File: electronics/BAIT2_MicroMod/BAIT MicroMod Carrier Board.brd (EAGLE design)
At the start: 92.7 x 80 mm, 156 parts, among them J1 SJ-43516-SMT, J10 QWIIC_RIGHT_ANGLE, J11 QWIIC_RIGHT_ANGLE, J15 BM05B-SRSS-TB(LF)(SN), J2 ST-TF-003A, J4 BM05B-SRSS-TB(LF)(SN), J5 QWIIC_RIGHT_ANGLE, J6 JST 2PH, J7 MICROMOD-2222-C, SW1 SKQGADE010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

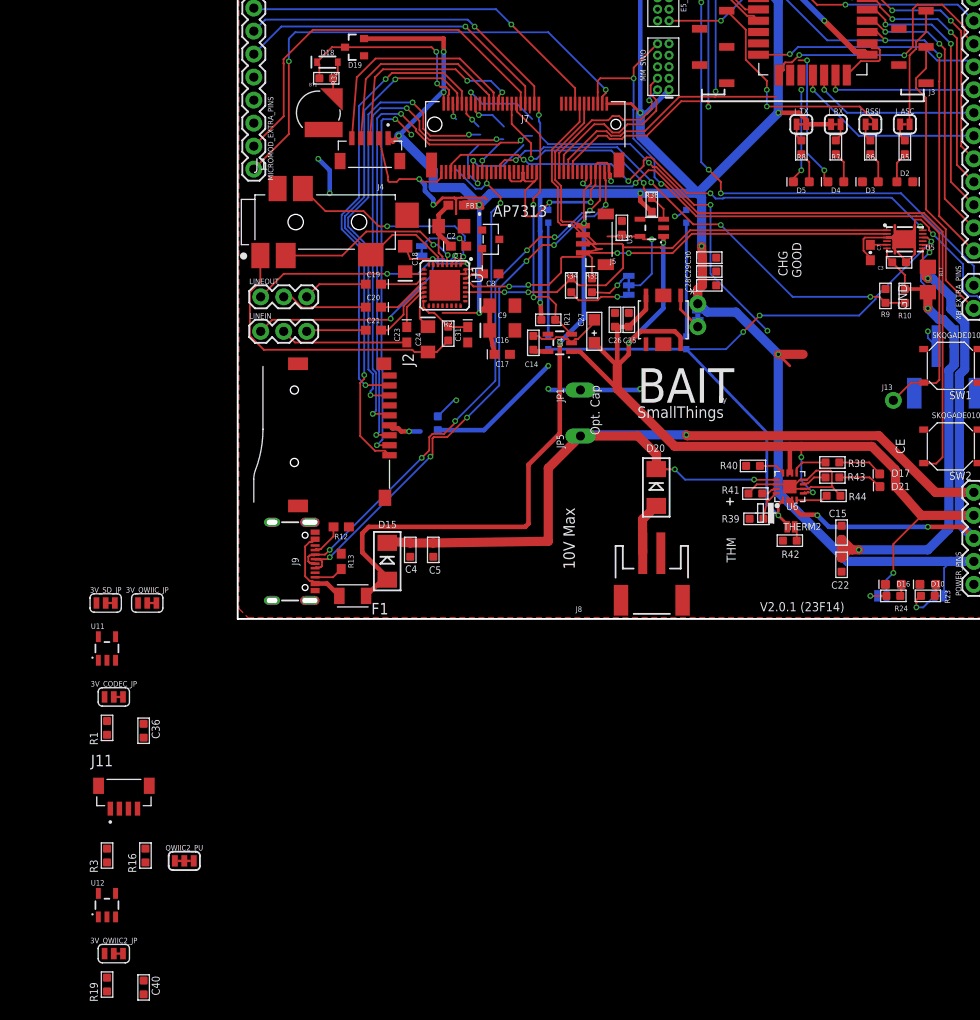
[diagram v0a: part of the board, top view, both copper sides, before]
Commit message: Connected SD card detect pin to micromod
Resolves #25
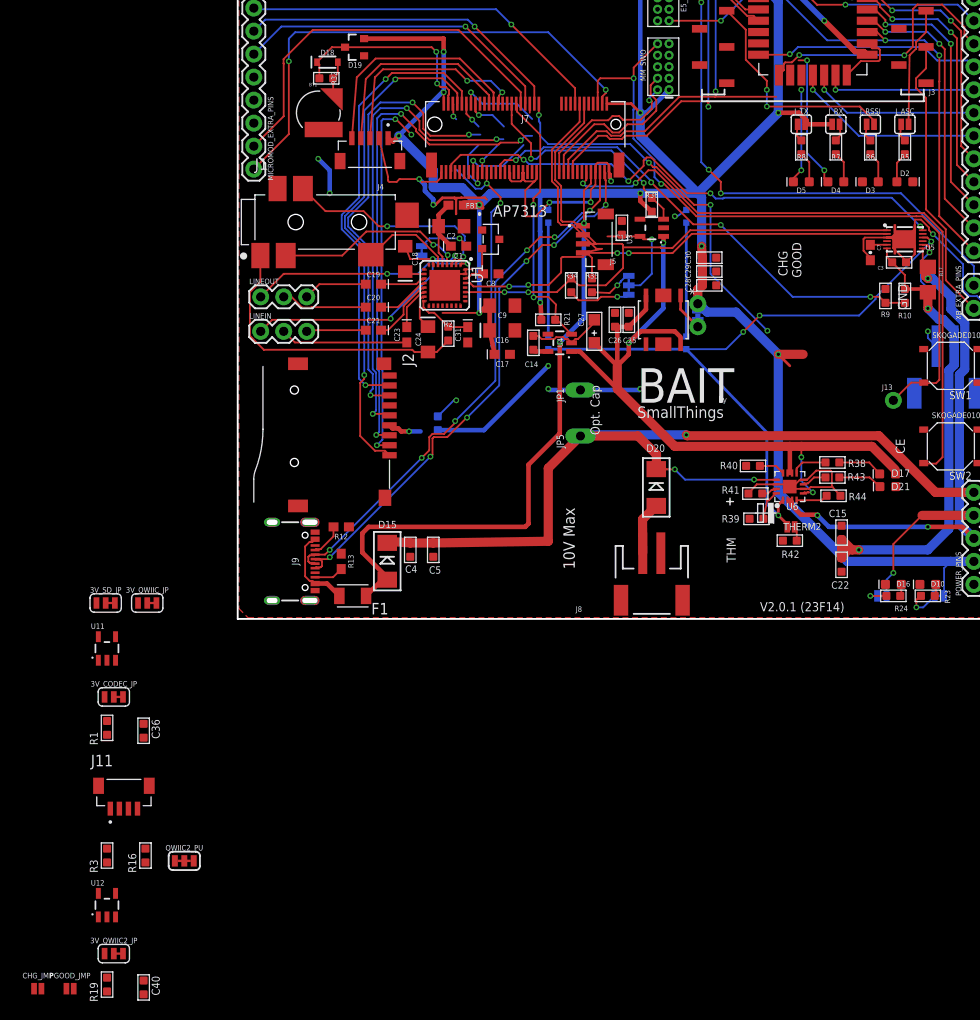
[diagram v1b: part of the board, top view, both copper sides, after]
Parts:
- added CHG_JMP, PGOOD_JMP: (no value), SparkFun-Jumpers:SMT-JUMPER_2_NO_NO-SILK
- J_ASC, J_RSSI, J_RX, J_TX: value (none) -> JUMPER-SMT_2_NO_SILK; device SparkFun-Jumpers:SMT-JUMPER_2_NC_TRACE_SILK -> SparkFun-Jumpers:SMT-JUMPER_2_NO_SILK
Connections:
- new net N$75: D21.A, PGOOD_JMP.1
- new net N$76: CHG_JMP.1, D17.A
- new net SD_DETECT: J2.9, J7.73
- net V+: now also CHG_JMP.2, PGOOD_JMP.2; no longer D17.A, D21.A
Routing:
- net V+: track 113.7 -> 107.5 mm
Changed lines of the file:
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@@
 <attribute name="NAME" x="19.251" y="75.865" size="0.889" layer="25" ratio="11" rot="R90"/>
 </element>
-<element name="J_ASC" library="SparkFun-Jumpers" package="SMT-JUMPER_2_NC_TRACE_SILK" package3d_urn="urn:adsk.eagle:package:39281/1" value="" x="73.66" y="54.61" smashed="yes" grouprefs="WIRELESS">
+<element name="J_ASC" library="SparkFun-Jumpers" library_urn="urn:adsk.eagle:library:528" package="SMT-JUMPER_2_NO_SILK" package3d_urn="urn:adsk.eagle:package:39279/1" value="JUMPER-SMT_2_NO_SILK" x="73.66" y="54.61" smashed="yes" grouprefs="WIRELESS">
 <attribute name="NAME" x="73.66" y="55.753" size="0.6096" layer="25" font="vector" ratio="20" align="bottom-center"/>
 <attribute name="VALUE" x="73.66" y="53.467" size="0.6096" layer="27" font="vector" ratio="20" align="top-center"/>
@@
 <attribute name="PROD_ID" value="HW-14899" x="137.414" y="-20.574" size="1.778" layer="27" display="off"/>
 </element>
-<element name="J_RX" library="SparkFun-Jumpers" package="SMT-JUMPER_2_NC_TRACE_SILK" package3d_urn="urn:adsk.eagle:package:39281/1" value="" x="66.04" y="54.61" smashed="yes" grouprefs="WIRELESS">
+<element name="J_RX" library="SparkFun-Jumpers" library_urn="urn:adsk.eagle:library:528" package="SMT-JUMPER_2_NO_SILK" package3d_urn="urn:adsk.eagle:package:39279/1" value="JUMPER-SMT_2_NO_SILK" x="66.04" y="54.61" smashed="yes" grouprefs="WIRELESS">
 <attribute name="NAME" x="66.04" y="55.753" size="0.6096" layer="25" font="vector" ratio="20" align="bottom-center"/>
 <attribute name="VALUE" x="66.04" y="53.467" size="0.6096" layer="27" font="vector" ratio="20" align="top-center"/>
@@
 <attribute name="VALUE" x="3.81" y="48.387" size="0.6096" layer="27" font="vector" ratio="20" rot="R90"/>
 </element>
-<element name="J_TX" library="SparkFun-Jumpers" package="SMT-JUMPER_2_NC_TRACE_SILK" package3d_urn="urn:adsk.eagle:package:39281/1" value="" x="62.23" y="54.61" smashed="yes" grouprefs="WIRELESS">
+<element name="J_TX" library="SparkFun-Jumpers" library_urn="urn:adsk.eagle:library:528" package="SMT-JUMPER_2_NO_SILK" package3d_urn="urn:adsk.eagle:package:39279/1" value="JUMPER-SMT_2_NO_SILK" x="62.23" y="54.61" smashed="yes" grouprefs="WIRELESS">
 <attribute name="NAME" x="62.23" y="55.753" size="0.6096" layer="25" font="vector" ratio="20" align="bottom-center"/>
 <attribute name="VALUE" x="62.23" y="53.467" size="0.6096" layer="27" font="vector" ratio="20" align="top-center"/>
@@
 <attribute name="NAME" x="71.52" y="33.322" size="0.6096" layer="25" font="vector" ratio="20" align="bottom-center"/>
 </element>
-<element name="J_RSSI" library="SparkFun-Jumpers" package="SMT-JUMPER_2_NC_TRACE_SILK" package3d_urn="urn:adsk.eagle:package:39281/1" value="" x="69.85" y="54.61" smashed="yes" grouprefs="WIRELESS">
+<element name="J_RSSI" library="SparkFun-Jumpers" library_urn="urn:adsk.eagle:library:528" package="SMT-JUMPER_2_NO_SILK" package3d_urn="urn:adsk.eagle:package:39279/1" value="JUMPER-SMT_2_NO_SILK" x="69.85" y="54.61" smashed="yes" grouprefs="WIRELESS">
 <attribute name="NAME" x="69.85" y="55.753" size="0.6096" layer="25" font="vector" ratio="20" align="bottom-center"/>
 <attribute name="VALUE" x="69.85" y="53.467" size="0.6096" layer="27" font="vector" ratio="20" align="top-center"/>
@@
 <attribute name="VALUE" x="-13.679" y="-38.099" size="0.6096" layer="27" font="vector" ratio="20" align="top-center"/>
 </element>
+<element name="PGOOD_JMP" library="SparkFun-Jumpers" library_urn="urn:adsk.eagle:library:528" package="SMT-JUMPER_2_NO_NO-SILK" package3d_urn="urn:adsk.eagle:package:39277/1" value="" x="-18.508" y="-40.83" smashed="yes">
+<attribute name="NAME" x="-18.508" y="-39.687" size="0.6096" layer="25" font="vector" ratio="20" align="bottom-center"/>
+<attribute name="VALUE" x="-18.508" y="-41.973" size="0.6096" layer="27" font="vector" ratio="20" align="top-center"/>
+</element>
+<element name="CHG_JMP" library="SparkFun-Jumpers" library_urn="urn:adsk.eagle:library:528" package="SMT-JUMPER_2_NO_NO-SILK" package3d_urn="urn:adsk.eagle:package:39277/1" value="" x="-22.077" y="-40.83" smashed="yes">
+<attribute name="NAME" x="-22.077" y="-39.687" size="0.6096" layer="25" font="vector" ratio="20" align="bottom-center"/>
+<attribute name="VALUE" x="-22.077" y="-41.973" size="0.6096" layer="27" font="vector" ratio="20" align="top-center"/>
+</element>
 </elements>
 <signals>
@@
 <wire x1="44.45" y1="46.14" x2="44.45" y2="46.99" width="0.508" layer="1"/>
 <via x="44.45" y="46.99" extent="1-16" drill="0.35"/>
-<wire x1="62.7507" y1="54.61" x2="62.8269" y2="54.61" width="0.508" layer="1"/>
-<wire x1="62.8269" y1="54.61" x2="65.5193" y2="54.61" width="0.508" layer="1"/>
+<wire x1="62.6364" y1="54.61" x2="62.8269" y2="54.61" width="0.508" layer="1"/>
+<wire x1="62.8269" y1="54.61" x2="65.6336" y2="54.61" width="0.508" layer="1"/>
 <wire x1="59.69" y1="55.88" x2="59.69" y2="68.199" width="1.016" layer="16"/>
 <wire x1="59.69" y1="68.199" x2="56.642" y2="71.247" width="1.016" layer="16"/>
@@
 <wire x1="58.42" y1="58.42" x2="58.42" y2="56.5686" width="0.2032" layer="16"/>
 <via x="58.42" y="56.5686" extent="1-16" drill="0.35"/>
-<wire x1="70.2945" y1="54.6862" x2="70.3707" y2="54.61" width="0.2032" layer="1"/>
+<wire x1="70.2945" y1="54.6862" x2="70.2564" y2="54.61" width="0.2032" layer="1"/>
 <wire x1="58.42" y1="56.5686" x2="68.6951125" y2="56.5686" width="0.2032" layer="1"/>
 <wire x1="68.6951125" y1="56.5686" x2="70.2945" y2="54.9692125" width="0.2032" layer="1"/>
@@
 <wire x1="76" y1="64.7842125" x2="74.896" y2="63.6802125" width="0.2032" layer="1"/>
 <wire x1="74.896" y1="62.9453" x2="74.1807" y2="62.23" width="0.2032" layer="1"/>
-<wire x1="74.1807" y1="62.23" x2="74.1807" y2="54.61" width="0.2032" layer="1"/>
+<wire x1="74.1807" y1="62.23" x2="74.0664" y2="54.61" width="0.2032" layer="1"/>
 <wire x1="74.896" y1="63.6802125" x2="74.896" y2="62.9453" width="0.2032" layer="1"/>
 </signal>
@@
 <contactref element="J_ASC" pad="1"/>
 <wire x1="73.66" y1="52.832" x2="73.1393" y2="53.3527" width="0.2032" layer="1"/>
-<wire x1="73.1393" y1="53.3527" x2="73.1393" y2="54.61" width="0.2032" layer="1"/>
+<wire x1="73.1393" y1="53.3527" x2="73.2536" y2="54.61" width="0.2032" layer="1"/>
 </signal>
 <signal name="N$34">
@@
 <contactref element="R6" pad="2"/>
 <contactref element="J_RSSI" pad="1"/>
-<wire x1="69.3293" y1="54.61" x2="69.3293" y2="53.3527" width="0.2032" layer="1"/>
+<wire x1="69.4436" y1="54.61" x2="69.3293" y2="53.3527" width="0.2032" layer="1"/>
 <wire x1="69.3293" y1="53.3527" x2="69.85" y2="52.832" width="0.2032" layer="1"/>
 </signal>
@@
 <contactref element="R8" pad="2"/>
 <contactref element="J_TX" pad="1"/>
-<wire x1="61.7093" y1="54.61" x2="61.7093" y2="53.3527" width="0.2032" layer="1"/>
+<wire x1="61.8236" y1="54.61" x2="61.7093" y2="53.3527" width="0.2032" layer="1"/>
 <wire x1="61.7093" y1="53.3527" x2="62.23" y2="52.832" width="0.2032" layer="1"/>
 </signal>
@@
 </signal>
 <signal name="V+" class="1">
-<contactref element="D21" pad="A"/>
-<contactref element="D17" pad="A"/>
 <contactref element="VIN_LED2" pad="2"/>
 <contactref element="U3" pad="1"/>
@@
 <contactref element="U4" pad="1"/>
 <wire x1="81.28" y1="11.43" x2="75.553" y2="11.43" width="1.016" layer="1"/>
-<wire x1="75.499809375" y1="11.376809375" x2="72.659" y2="14.605" width="1.016" layer="1"/>
-<wire x1="72.659" y1="14.605" x2="72.632" y2="14.902" width="1.016" layer="1"/>
-<wire x1="72.632" y1="14.902" x2="72.632" y2="16.002" width="1.016" layer="1"/>
-<wire x1="72.632" y1="16.002" x2="72.59595" y2="16.47405" width="1.016" layer="1"/>
 <wire x1="72.59595" y1="16.47405" x2="70.02" y2="19.05" width="1.016" layer="1"/>
 <wire x1="70.02" y1="19.05" x2="62.23" y2="19.05" width="1.016" layer="1"/>
@@
 <contactref element="U11" pad="1"/>
 <contactref element="U12" pad="1"/>
+<contactref element="PGOOD_JMP" pad="2"/>
+<contactref element="CHG_JMP" pad="2"/>
+<wire x1="72.59595" y1="16.47405" x2="81.28" y2="11.43" width="0" layer="19" extent="1-1"/>
 <wire x1="-15.386" y1="-4.5661" x2="36.8601" y2="29.53" width="0" layer="19" extent="1-1"/>
 <wire x1="-15.386" y1="-32.9061" x2="-15.386" y2="-4.5661" width="0" layer="19" extent="1-1"/>
+<wire x1="-18.1016" y1="-40.83" x2="-15.386" y2="-32.9061" width="0" layer="19" extent="1-1"/>
+<wire x1="-21.6706" y1="-40.83" x2="-18.1016" y2="-40.83" width="0" layer="19" extent="1-1"/>
 </signal>
 <signal name="1.8V" class="1">
@@
 <contactref element="R7" pad="2"/>
 <wire x1="66.04" y1="52.832" x2="66.5607" y2="53.4407" width="0.2032" layer="1"/>
-<wire x1="66.5607" y1="53.4407" x2="66.5607" y2="54.61" width="0.2032" layer="1"/>
+<wire x1="66.5607" y1="53.4407" x2="66.4464" y2="54.61" width="0.2032" layer="1"/>
 </signal>
 <signal name="N$10">
@@
 <contactref element="J7" pad="51"/>
 </signal>
+<signal name="N$75">
+<contactref element="PGOOD_JMP" pad="1"/>
+<contactref element="D21" pad="A"/>
+<wire x1="-18.9144" y1="-40.83" x2="72.659" y2="14.605" width="0" layer="19" extent="1-1"/>
+</signal>
+<signal name="N$76">
+<contactref element="CHG_JMP" pad="1"/>
+<contactref element="D17" pad="A"/>
+<wire x1="-22.4834" y1="-40.83" x2="72.632" y2="16.002" width="0" layer="19" extent="1-1"/>
+</signal>
+<signal name="SD_DETECT">
+<contactref element="J2" pad="9"/>
+<contactref element="J7" pad="73"/>
+<wire x1="16.76" y1="26.87" x2="23" y2="49.335" width="0" layer="19" extent="1-1"/>
+</signal>
 </signals>

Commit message: Connect headphone switches to teensy ports
Resolves #24
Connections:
- new net HP_RING_SW_NC: J1.6, J7.69
- new net HP_TIP_SW_NC: J1.5, J7.67
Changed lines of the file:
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@@
 <wire x1="16.76" y1="26.87" x2="23" y2="49.335" width="0" layer="19" extent="1-1"/>
+</signal>
+<signal name="HP_RING_SW_NC">
+<contactref element="J1" pad="6"/>
+<contactref element="J7" pad="69"/>
+<wire x1="4.402" y1="47.515" x2="24" y2="49.335" width="0" layer="19" extent="1-1"/>
+</signal>
+<signal name="HP_TIP_SW_NC">
+<contactref element="J1" pad="5"/>
+<contactref element="J7" pad="67"/>
+<wire x1="18.702" y1="44.565" x2="24.5" y2="49.335" width="0" layer="19" extent="1-1"/>
 </signal>
 </signals>

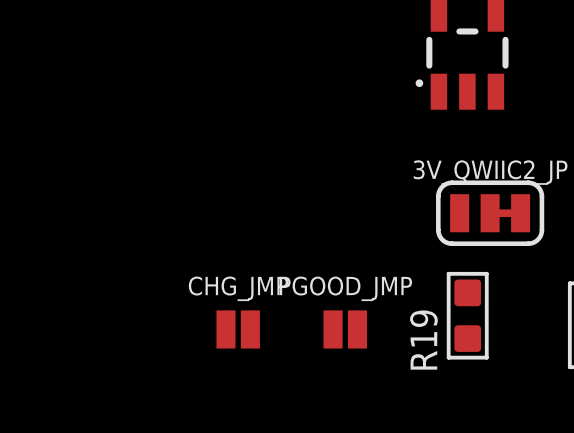
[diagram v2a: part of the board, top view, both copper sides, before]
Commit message: Updates pin 24 connection on WIO
Solves #8
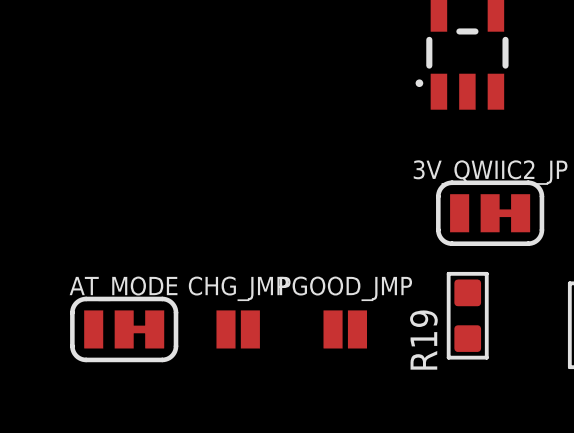
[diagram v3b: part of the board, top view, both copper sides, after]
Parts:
- added AT_MODE: MK2_LR, SparkFun-Jumpers:SMT-JUMPER_3_1-NC_TRACE_SILK
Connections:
- net 3.3V: now also AT_MODE.3
- net GND: now also AT_MODE.1
- net PB13/BOOT/SCK: now also AT_MODE.2
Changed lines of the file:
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@@
 <drawing>
 <settings>
-<setting alwaysvectorfont="yes"/>
+<setting alwaysvectorfont="no"/>
 <setting verticaltext="up"/>
 </settings>
@@
 <element name="C10" library="OPL_Capacitor" library_urn="urn:adsk.eagle:library:8004261" package="C0603" package3d_urn="urn:adsk.eagle:package:8004287/1" value="4.7uf" x="57.15" y="73.66" smashed="yes" rot="R270" grouprefs="WIRELESS">
 <attribute name="MPN" value="CC0603KRX5R6BB475" x="57.15" y="73.66" size="1.778" layer="27" rot="R270" display="off"/>
+<attribute name="NAME" x="56.315" y="70.335" size="0.889" layer="25" ratio="11" rot="R90"/>
 <attribute name="NAME" x="56.896" y="74.93" size="0.635" layer="33" ratio="10" rot="R270"/>
-<attribute name="NAME" x="56.315" y="70.335" size="0.889" layer="25" ratio="11" rot="R90"/>
 <attribute name="VALUE" value="4.7uf" x="56.24" y="75.0135" size="0.635" layer="27" ratio="10" align="center"/>
 </element>
@@
 <element name="C33" library="Discrete-new" package="C0603" value="4.7uF" x="49.276" y="76.327" smashed="yes" rot="R90">
 <attribute name="MPN" value="TMCJ0J475MTRF" x="49.276" y="76.327" size="1.778" layer="27" rot="R90" display="off"/>
+<attribute name="NAME" x="49.53" y="75.057" size="0.635" layer="33" ratio="10" rot="R90"/>
 <attribute name="NAME" x="48.641" y="74.422" size="0.889" layer="25" ratio="11" rot="R90"/>
-<attribute name="NAME" x="49.53" y="75.057" size="0.635" layer="33" ratio="10" rot="R90"/>
 <attribute name="VALUE" x="49.2125" y="76.327" size="0.635" layer="27" ratio="10" rot="R90" align="center"/>
 </element>
@@
 <element name="C38" library="OPL_Capacitor" library_urn="urn:adsk.eagle:library:8004261" package="C0603" package3d_urn="urn:adsk.eagle:package:8004287/1" value="100nf" x="90.17" y="41.91" smashed="yes" rot="MR0">
 <attribute name="MPN" value="CC0603KRX7R9BB104" x="90.17" y="41.91" size="1.778" layer="28" rot="MR0" display="off"/>
+<attribute name="NAME" x="90.424" y="43.18" size="0.635" layer="34" ratio="10" rot="MR270"/>
 <attribute name="NAME" x="89.281" y="43.18" size="0.889" layer="26" ratio="11" rot="MR270"/>
-<attribute name="NAME" x="90.424" y="43.18" size="0.635" layer="34" ratio="10" rot="MR270"/>
 <attribute name="VALUE" x="91.7575" y="43.18" size="0.635" layer="28" ratio="10" rot="MR270"/>
 </element>
@@
 <element name="C36" library="OPL_Capacitor" library_urn="urn:adsk.eagle:library:8004261" package="C0603" package3d_urn="urn:adsk.eagle:package:8004287/1" value="1uf" x="-10.387" y="-12.35" smashed="yes">
 <attribute name="MPN" value="CC0603KRX7R8BB105" x="-18.892" y="2.816" size="1.778" layer="27" display="off"/>
+<attribute name="NAME" x="-9.498" y="-11.08" size="0.889" layer="25" ratio="11" rot="R270"/>
 <attribute name="NAME" x="-10.641" y="-11.08" size="0.635" layer="33" ratio="10" rot="R270"/>
-<attribute name="NAME" x="-9.498" y="-11.08" size="0.889" layer="25" ratio="11" rot="R270"/>
 <attribute name="VALUE" x="-11.9745" y="-11.08" size="0.635" layer="27" ratio="10" rot="R270"/>
 </element>
@@
 <element name="C40" library="OPL_Capacitor" library_urn="urn:adsk.eagle:library:8004261" package="C0603" package3d_urn="urn:adsk.eagle:package:8004287/1" value="1uf" x="-10.387" y="-40.69" smashed="yes">
 <attribute name="MPN" value="CC0603KRX7R8BB105" x="-18.892" y="-25.524" size="1.778" layer="27" display="off"/>
+<attribute name="NAME" x="-9.498" y="-39.42" size="0.889" layer="25" ratio="11" rot="R270"/>
 <attribute name="NAME" x="-10.641" y="-39.42" size="0.635" layer="33" ratio="10" rot="R270"/>
-<attribute name="NAME" x="-9.498" y="-39.42" size="0.889" layer="25" ratio="11" rot="R270"/>
 <attribute name="VALUE" x="-11.9745" y="-39.42" size="0.635" layer="27" ratio="10" rot="R270"/>
 </element>
@@
 <attribute name="NAME" x="-22.077" y="-39.687" size="0.6096" layer="25" font="vector" ratio="20" align="bottom-center"/>
 <attribute name="VALUE" x="-22.077" y="-41.973" size="0.6096" layer="27" font="vector" ratio="20" align="top-center"/>
+</element>
+<element name="AT_MODE" library="SparkFun-Jumpers" library_urn="urn:adsk.eagle:library:528" package="SMT-JUMPER_3_1-NC_TRACE_SILK" package3d_urn="urn:adsk.eagle:package:39288/1" value="MK2_LR" x="-25.877" y="-40.83" smashed="yes">
+<attribute name="NAME" x="-25.877" y="-39.687" size="0.6096" layer="25" font="vector" ratio="20" align="bottom-center"/>
+<attribute name="VALUE" x="-25.877" y="-41.973" size="0.6096" layer="27" font="vector" ratio="20" align="top-center"/>
 </element>
 </elements>
@@
 <contactref element="C40" pad="2"/>
 <contactref element="U12" pad="2"/>
+<contactref element="AT_MODE" pad="1"/>
 <wire x1="69.5" y1="63.54" x2="67.25" y2="72.04" width="0" layer="19" extent="1-1"/>
 <wire x1="57.912" y1="73.66" x2="67.25" y2="72.04" width="0" layer="19" extent="1-1"/>
@@
 <wire x1="-14.436" y1="-32.9061" x2="-14.064" y2="-20.95" width="0" layer="19" extent="1-1"/>
 <wire x1="-10.387" y1="-41.452" x2="-14.436" y2="-32.9061" width="0" layer="19" extent="1-1"/>
+<wire x1="-26.893" y1="-40.83" x2="-14.436" y2="-32.9061" width="0" layer="19" extent="1-1"/>
 </signal>
 <signal name="3.3V" class="1">
@@
 <contactref element="R19" pad="2"/>
 <contactref element="3V_QWIIC2_JP" pad="1"/>
-<wire x1="-11.004" y1="1.755" x2="22.61" y2="33.782" width="0" layer="19" extent="1-1"/>
-<wire x1="-15.593" y1="1.755" x2="-11.004" y2="1.755" width="0" layer="19" extent="1-1"/>
-<wire x1="-14.695" y1="-8.616" x2="-15.593" y2="1.755" width="0" layer="19" extent="1-1"/>
-<wire x1="-14.426" y1="-12.795" x2="-14.695" y2="-8.616" width="0" layer="19" extent="1-1"/>
-<wire x1="-14.695" y1="-36.956" x2="-14.426" y2="-12.795" width="0" layer="19" extent="1-1"/>
-<wire x1="-14.426" y1="-41.135" x2="-14.695" y2="-36.956" width="0" layer="19" extent="1-1"/>
+<contactref element="AT_MODE" pad="3"/>
+<wire x1="-14.426" y1="-41.135" x2="-24.861" y2="-40.83" width="0" layer="19" extent="1-1"/>
+<wire x1="-14.695" y1="-36.956" x2="-14.426" y2="-41.135" width="0" layer="19" extent="1-1"/>
+<wire x1="-14.426" y1="-12.795" x2="-14.695" y2="-36.956" width="0" layer="19" extent="1-1"/>
+<wire x1="-14.695" y1="-8.616" x2="-14.426" y2="-12.795" width="0" layer="19" extent="1-1"/>
+<wire x1="-15.593" y1="1.755" x2="-14.695" y2="-8.616" width="0" layer="19" extent="1-1"/>
+<wire x1="-11.004" y1="1.755" x2="-15.593" y2="1.755" width="0" layer="19" extent="1-1"/>
+<wire x1="22.61" y1="33.782" x2="-11.004" y2="1.755" width="0" layer="19" extent="1-1"/>
 </signal>
 <signal name="USB_D-">
@@
 <contactref element="U7" pad="24"/>
 <contactref element="E5_EXTRA_PINS" pad="2"/>
+<contactref element="AT_MODE" pad="2"/>
+<wire x1="-25.877" y1="-40.83" x2="64.75" y2="72.04" width="0" layer="19" extent="1-1"/>
 </signal>
 <signal name="PA14/SWCLK">
